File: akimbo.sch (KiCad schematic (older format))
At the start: 71 parts, among them J1 USB mini-B, J2 3.5mm TRRS, J3 3.5mm TRRS, K1 -, K11 -, K12 -, K13 -, K14 -, K15 -, K16 -, K17 -, K18 -, K19 -, K2 -, K20 -, K21 -, K22 -, K23 -, K24 -, K25 -, K26 -, K27 -, K28 -, K29 -, K3 -, K30 -, K4 -, K6 -, K7 -, K8 -, K9 -, U1 ATmega32U4, U2 MCP23017_SO, Y1 16M

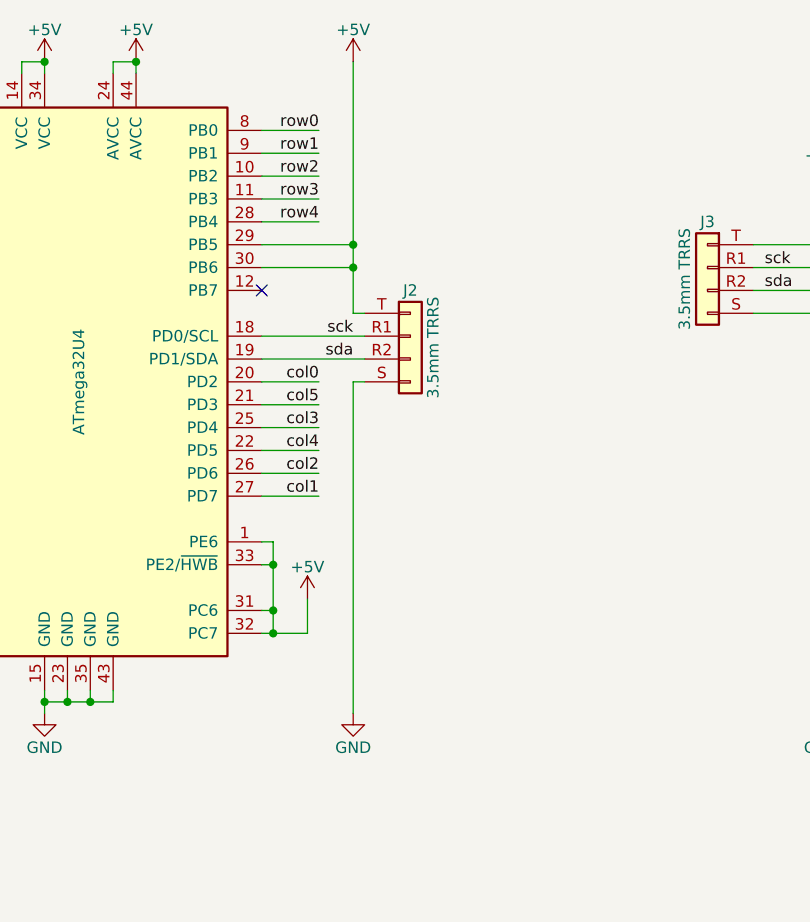
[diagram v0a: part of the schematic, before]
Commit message: I2C pullups
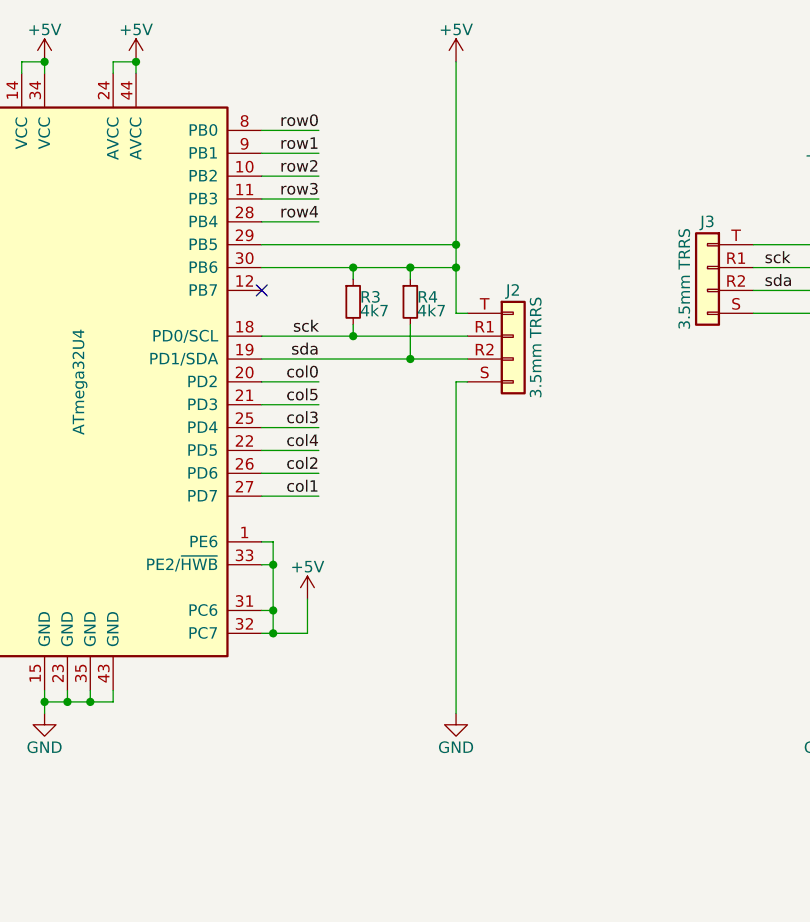
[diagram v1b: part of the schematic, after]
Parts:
- added R3, R4: 4k7, Resistor_SMD:R_0805_2012Metric_Pad1.15x1.40mm_HandSolder, symbol Device:R_Small
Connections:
- net +5V: now also R3.1, R4.1
- net sck: now also R3.2
- net sda: now also R4.2
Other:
- moved on the sheet: J2
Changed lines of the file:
@@
 L power:GND #PWR05
 U 1 1 5C498A21
-P 4750 4850
-F 0 "#PWR05" H 4750 4600 50  0001 C CNN
-F 1 "GND" H 4750 4700 50  0000 C CNN
-F 2 "" H 4750 4850 50  0001 C CNN
-F 3 "" H 4750 4850 50  0001 C CNN
-	1    4750 4850
+P 5200 4850
+F 0 "#PWR05" H 5200 4600 50  0001 C CNN
+F 1 "GND" H 5200 4700 50  0000 C CNN
+F 2 "" H 5200 4850 50  0001 C CNN
+F 3 "" H 5200 4850 50  0001 C CNN
+	1    5200 4850
 	1    0    0    -1
 $EndComp
@@
 L power:+5V #PWR04
 U 1 1 5C49863E
-P 4750 2000
-F 0 "#PWR04" H 4750 1850 50  0001 C CNN
-F 1 "+5V" H 4750 2140 50  0000 C CNN
-F 2 "" H 4750 2000 50  0001 C CNN
-F 3 "" H 4750 2000 50  0001 C CNN
-	1    4750 2000
+P 5200 2000
+F 0 "#PWR04" H 5200 1850 50  0001 C CNN
+F 1 "+5V" H 5200 2140 50  0000 C CNN
+F 2 "" H 5200 2000 50  0001 C CNN
+F 3 "" H 5200 2000 50  0001 C CNN
+	1    5200 2000
 	1    0    0    -1
 $EndComp
@@
 	6800 3100 6800 4850
 Wire Wire Line
-	4750 2000 4750 2800
-Wire Wire Line
-	4750 3400 4750 4850
-Wire Wire Line
-	4750 3100 4800 3100
-Wire Wire Line
-	4800 3400 4750 3400
-Wire Wire Line
-	4350 3300 4800 3300
-Wire Wire Line
-	4350 3200 4800 3200
+	5200 2000 5200 2800
+Wire Wire Line
+	5200 3400 5200 4850
+Wire Wire Line
+	5200 3100 5250 3100
+Wire Wire Line
+	5250 3400 5200 3400
+Wire Wire Line
+	4350 3300 5000 3300
+Wire Wire Line
+	4350 3200 4750 3200
 $Comp
 L akimbo:Conn_TRRS J2
 U 1 1 5C433D7B
-P 5000 3200
-F 0 "J2" H 5000 3400 50  0000 C CNN
-F 1 "3.5mm TRRS" V 5100 3150 50  0000 C CNN
-F 2 "Connector_Audio:Jack_3.5mm_PJ320D_Horizontal" H 5000 3200 50  0001 C CNN
-F 3 "~" H 5000 3200 50  0001 C CNN
-	1    5000 3200
+P 5450 3200
+F 0 "J2" H 5450 3400 50  0000 C CNN
+F 1 "3.5mm TRRS" V 5550 3150 50  0000 C CNN
+F 2 "Connector_Audio:Jack_3.5mm_PJ320D_Horizontal" H 5450 3200 50  0001 C CNN
+F 3 "~" H 5450 3200 50  0001 C CNN
+	1    5450 3200
 	1    0    0    -1
 $EndComp
@@
 Text Label 6550 3000 0    50   ~ 0
 sda
-Text Label 4750 3200 2    50   ~ 0
+Text Label 4600 3200 2    50   ~ 0
 sck
-Text Label 4750 3300 2    50   ~ 0
+Text Label 4600 3300 2    50   ~ 0
 sda
 Wire Wire Line
@@
 Connection ~ 4400 4500
 Wire Wire Line
-	4350 2800 4750 2800
-Connection ~ 4750 2800
-Wire Wire Line
-	4750 2800 4750 2900
+	4350 2800 5200 2800
+Connection ~ 5200 2800
+Wire Wire Line
+	5200 2800 5200 2900
 Wire Wire Line
 	4350 2900 4750 2900
-Connection ~ 4750 2900
-Wire Wire Line
-	4750 2900 4750 3100
+Connection ~ 5200 2900
+Wire Wire Line
+	5200 2900 5200 3100
 Wire Wire Line
 	4350 3500 4600 3500
@@
 Text Notes 14490 10530 0    50   ~ 0
 Released subject to the terms of the\nCERN Open Hardware License, v1.2\nSee LICENSE in the git repository for\ndetails
+$Comp
+L Device:R_Small R4
+U 1 1 5D70310F
+P 5000 3050
+F 0 "R4" H 5030 3070 50  0000 L CNN
+F 1 "4k7" H 5030 3010 50  0000 L CNN
+F 2 "Resistor_SMD:R_0805_2012Metric_Pad1.15x1.40mm_HandSolder" H 5000 3050 50  0001 C CNN
+F 3 "~" H 5000 3050 50  0001 C CNN
+	1    5000 3050
+	1    0    0    -1
+$EndComp
+$Comp
+L Device:R_Small R3
+U 1 1 5D703CA4
+P 4750 3050
+F 0 "R3" H 4780 3070 50  0000 L CNN
+F 1 "4k7" H 4780 3010 50  0000 L CNN
+F 2 "Resistor_SMD:R_0805_2012Metric_Pad1.15x1.40mm_HandSolder" H 4750 3050 50  0001 C CNN
+F 3 "~" H 4750 3050 50  0001 C CNN
+	1    4750 3050
+	1    0    0    -1
+$EndComp
+Wire Wire Line
+	5000 2900 5000 2950
+Connection ~ 5000 2900
+Wire Wire Line
+	5000 2900 5200 2900
+Wire Wire Line
+	4750 2900 4750 2950
+Connection ~ 4750 2900
+Wire Wire Line
+	4750 2900 5000 2900
+Wire Wire Line
+	4750 3150 4750 3200
+Connection ~ 4750 3200
+Wire Wire Line
+	4750 3200 5250 3200
+Wire Wire Line
+	5000 3300 5000 3150
+Connection ~ 5000 3300
+Wire Wire Line
+	5000 3300 5250 3300
 $EndSCHEMATC

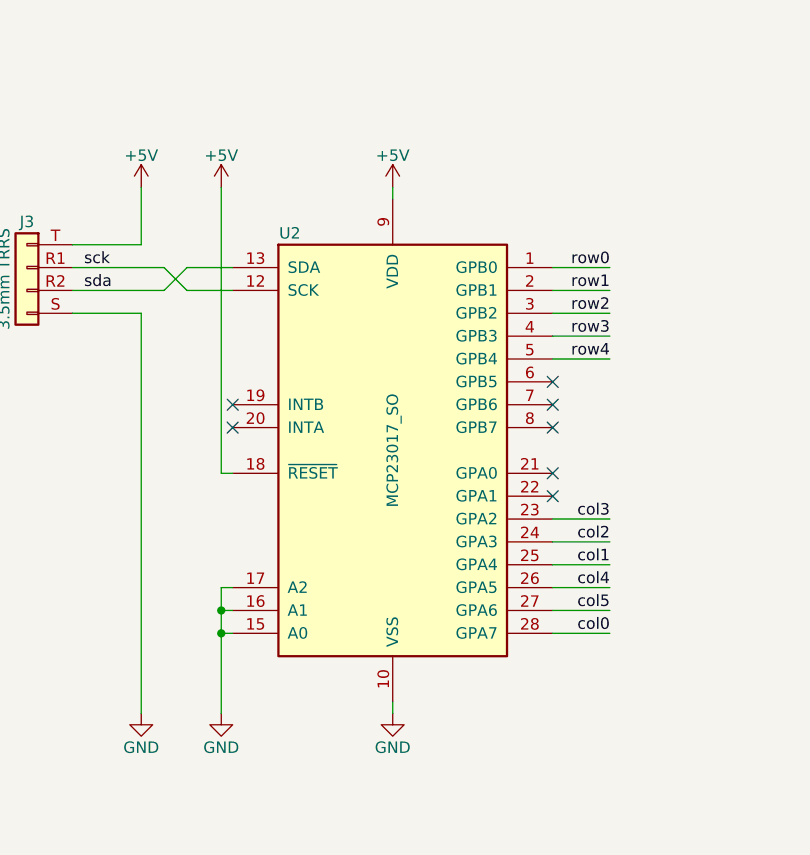
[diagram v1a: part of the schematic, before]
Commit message: replace mcp23017 with pca9995
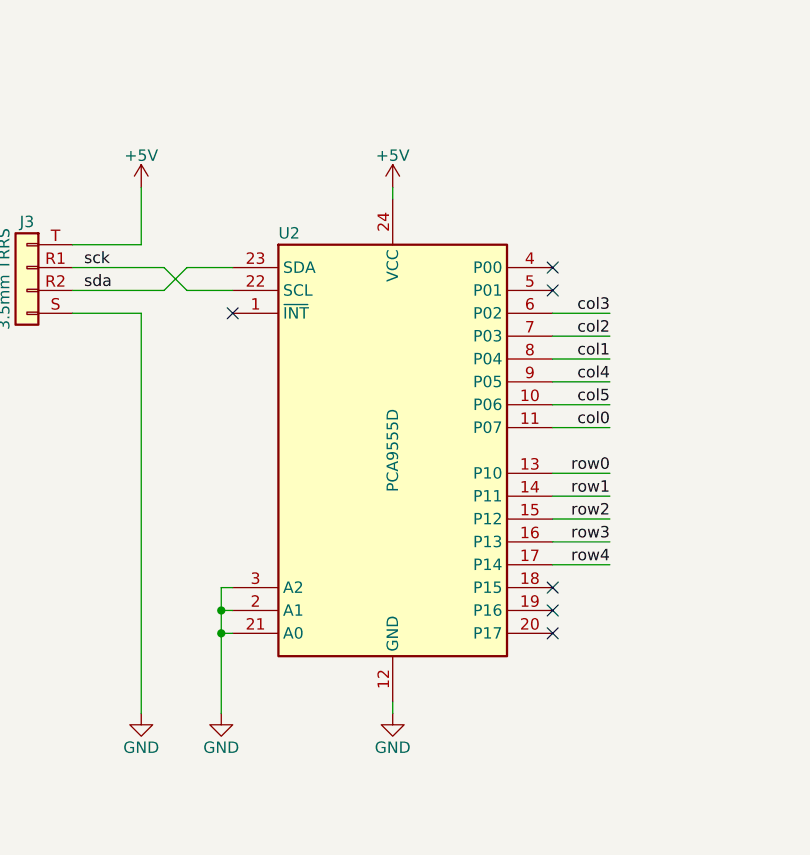
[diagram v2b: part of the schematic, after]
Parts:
- removed U2: MCP23017_SO, Package_SO:SOIC-28W_7.5x17.9mm_P1.27mm, symbol Interface_Expansion:MCP23017_SO
- added U2: PCA9555D, Package_SO:SOIC-24W_7.5x15.4mm_P1.27mm, symbol Interface_Expansion:TCA9555DBR
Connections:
- net +5V: now also U2.24 (VCC)
- net GND: now also U2.12 (GND), U2.2 (A1), U2.21 (A0), U2.3 (A2)
- net col0: now also U2.11 (P07)
- net col1: now also U2.8 (P04)
- net col2: now also U2.7 (P03)
- net col3: now also U2.6 (P02)
- net col4: now also U2.9 (P05)
- net col5: now also U2.10 (P06)
- net row0: now also U2.13 (P10)
- net row1: now also U2.14 (P11)
- net row2: now also U2.15 (P12)
- net row3: now also U2.16 (P13)
- net row4: now also U2.17 (P14)
- net sck: now also U2.22 (SCL)
- net sda: now also U2.23 (SDA)
- no-connect marks 10 -> 9
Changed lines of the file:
@@
 Wire Wire Line
 	3500 4800 3600 4800
-NoConn ~ 7200 3500
-NoConn ~ 7200 3600
+NoConn ~ 7200 3100
 Wire Wire Line
 	7900 2550 7900 2600
@@
 Wire Wire Line
 	7150 4500 7150 4850
+Text Label 8850 4100 2    50   ~ 0
+row3
+Text Label 8850 4200 2    50   ~ 0
+row4
+Wire Wire Line
+	8600 4000 8850 4000
+Wire Wire Line
+	8600 4100 8850 4100
+Wire Wire Line
+	8600 4200 8850 4200
+Text Label 8850 3600 2    50   ~ 0
+col0
+Text Label 8850 3300 2    50   ~ 0
+col1
 Text Label 8850 3200 2    50   ~ 0
-row3
-Text Label 8850 3300 2    50   ~ 0
-row4
+col2
+Text Label 8850 3100 2    50   ~ 0
+col3
+Text Label 8850 3400 2    50   ~ 0
+col4
+Text Label 8850 3500 2    50   ~ 0
+col5
+Wire Wire Line
+	8600 3600 8850 3600
+Wire Wire Line
+	8600 3300 8850 3300
+Wire Wire Line
+	8600 3200 8850 3200
 Wire Wire Line
 	8600 3100 8850 3100
 Wire Wire Line
-	8600 3200 8850 3200
-Wire Wire Line
-	8600 3300 8850 3300
-Text Label 8850 4500 2    50   ~ 0
-col0
-Text Label 8850 4200 2    50   ~ 0
-col1
-Text Label 8850 4100 2    50   ~ 0
-col2
-Text Label 8850 4000 2    50   ~ 0
-col3
-Text Label 8850 4300 2    50   ~ 0
-col4
-Text Label 8850 4400 2    50   ~ 0
-col5
-Wire Wire Line
-	8600 4500 8850 4500
-Wire Wire Line
-	8600 4200 8850 4200
-Wire Wire Line
-	8600 4100 8850 4100
-Wire Wire Line
-	8600 4000 8850 4000
-Wire Wire Line
-	8600 4300 8850 4300
-Wire Wire Line
-	8600 4400 8850 4400
-Wire Wire Line
-	7150 2550 7150 3800
-Wire Wire Line
-	7150 3800 7200 3800
-NoConn ~ 8600 3500
-NoConn ~ 8600 3600
+	8600 3400 8850 3400
+Wire Wire Line
+	8600 3500 8850 3500
 Wire Wire Line
 	11400 3850 11400 2750
@@
 Text Label 10650 5150 0    50   ~ 0
 row4
-NoConn ~ 8600 3400
 Text Label 4600 2300 2    50   ~ 0
 row0
@@
 	4350 2700 4600 2700
 NoConn ~ 4350 3000
-NoConn ~ 8600 3800
-NoConn ~ 8600 3900
 Wire Wire Line
 	7000 2900 7200 2900
@@
 $EndComp
 $Comp
-L power:+5V #PWR08
-U 1 1 5C8C4CC8
-P 7150 2550
-F 0 "#PWR08" H 7150 2400 50  0001 C CNN
-F 1 "+5V" H 7150 2690 50  0000 C CNN
-F 2 "" H 7150 2550 50  0001 C CNN
-F 3 "" H 7150 2550 50  0001 C CNN
-	1    7150 2550
-	1    0    0    -1
-$EndComp
-$Comp
 L power:GND #PWR09
 U 1 1 5C7E7653
@@
 F 3 "" H 7900 4850 50  0001 C CNN
 	1    7900 4850
-	1    0    0    -1
-$EndComp
-$Comp
-L Interface_Expansion:MCP23017_SO U2
-U 1 1 5C6D2688
-P 7900 3700
-F 0 "U2" H 7450 4650 50  0000 C CNN
-F 1 "MCP23017_SO" V 7900 3700 50  0000 C CNN
-F 2 "Package_SO:SOIC-28W_7.5x17.9mm_P1.27mm" H 8100 2700 50  0001 L CNN
-F 3 "http://ww1.microchip.com/downloads/en/DeviceDoc/20001952C.pdf" H 8100 2600 50  0001 L CNN
-	1    7900 3700
 	1    0    0    -1
 $EndComp
@@
 sda
 Wire Wire Line
-	8600 2900 8850 2900
-Text Label 8850 2900 2    50   ~ 0
+	8600 3800 8850 3800
+Text Label 8850 3800 2    50   ~ 0
 row0
 Wire Wire Line
-	8600 3000 8850 3000
-Text Label 8850 3000 2    50   ~ 0
+	8600 3900 8850 3900
+Text Label 8850 3900 2    50   ~ 0
 row1
 Wire Wire Line
@@
 Text Label 4600 3400 2    50   ~ 0
 col0
-Text Label 8850 3100 2    50   ~ 0
+Text Label 8850 4000 2    50   ~ 0
 row2
 $Comp
@@
 Wire Wire Line
 	5000 3300 5250 3300
+$Comp
+L Interface_Expansion:TCA9555DBR U2
+U 1 1 5D691C02
+P 7900 3700
+F 0 "U2" H 7400 4650 50  0000 L CNN
+F 1 "PCA9555D" V 7900 3700 50  0000 C CNN
+F 2 "Package_SO:SOIC-24W_7.5x15.4mm_P1.27mm" H 8950 2700 50  0001 C CNN
+F 3 "http://www.ti.com/lit/ds/symlink/tca9555.pdf" H 7400 4600 50  0001 C CNN
+	1    7900 3700
+	1    0    0    -1
+$EndComp
+NoConn ~ 8600 2900
+NoConn ~ 8600 3000
+NoConn ~ 8600 4300
+NoConn ~ 8600 4400
+NoConn ~ 8600 4500
 $EndSCHEMATC
